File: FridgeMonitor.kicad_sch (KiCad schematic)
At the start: 26 parts, among them J1 Conn_01x03, J2 Conn_01x03, J3 Conn_01x03, J4 Conn_01x03, J6 Conn_02x04_Odd_Even, J7 USB_B_Micro, U1 ESP-01v090, U2 LM2594M-3.3

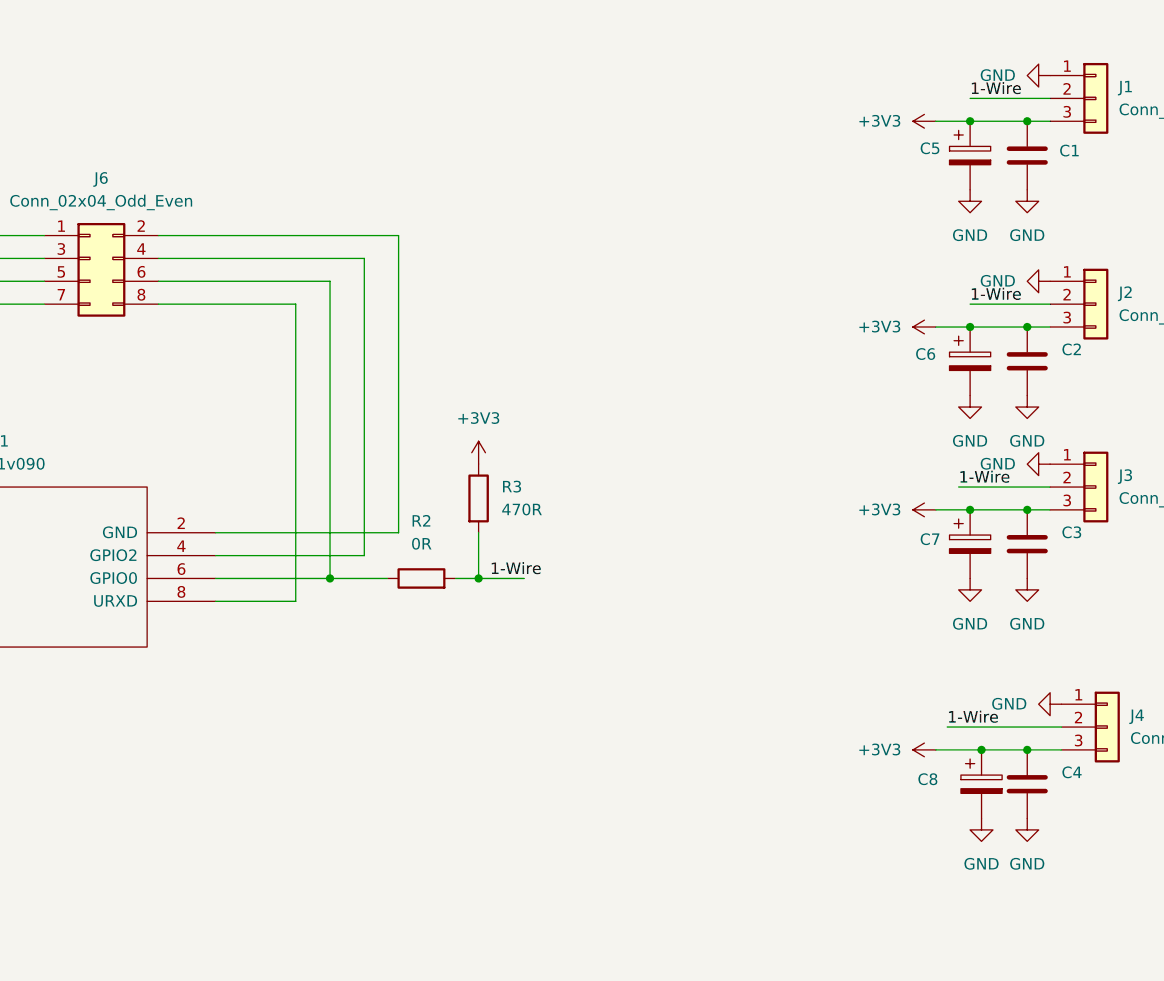
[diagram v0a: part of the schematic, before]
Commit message: For the moment all routed, except GND
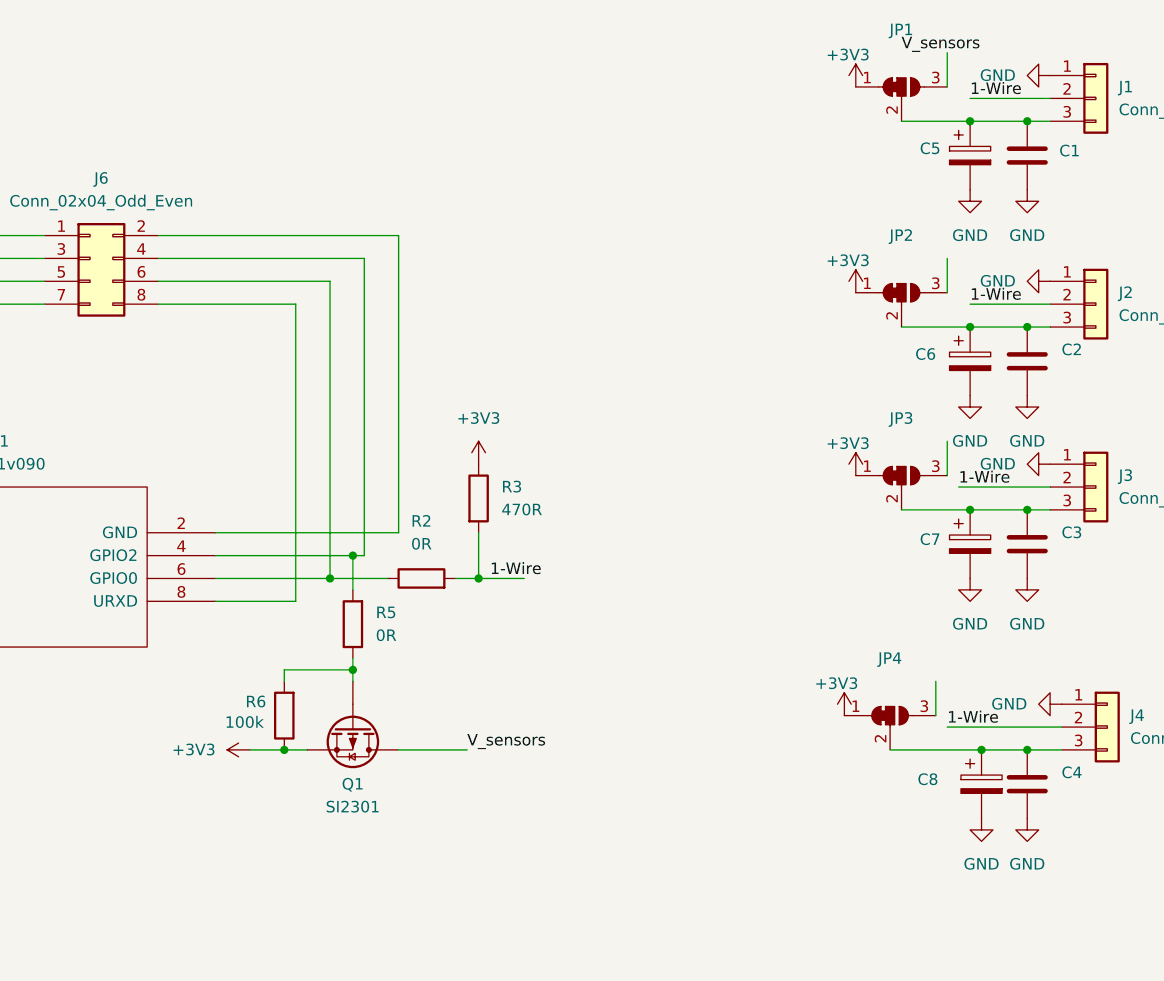
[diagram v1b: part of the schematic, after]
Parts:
- added JP1, JP2, JP3, JP4: SolderJumper_3_Bridged12, Jumper:SolderJumper-3_P1.3mm_Open_Pad1.0x1.5mm, symbol Jumper:SolderJumper_3_Bridged12
- added Q1: SI2301, Package_TO_SOT_SMD:TSOT-23, symbol Device:Q_PMOS
- added R5: 0R, Resistor_SMD:R_0805_2012Metric_Pad1.20x1.40mm_HandSolder, symbol Device:R
- added R6: 100k, Resistor_SMD:R_0805_2012Metric_Pad1.20x1.40mm_HandSolder, symbol Device:R
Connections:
- net +3V3: now also JP1.1 (A), JP2.1 (A), JP3.1 (A), JP4.1 (A), Q1.2 (S), R6.1; no longer C1.1, C2.1, C3.1, C4.1, C5.1, C6.1, C7.1, C8.1, J1.3 (Pin_3), J2.3 (Pin_3), J3.3 (Pin_3), J4.3 (Pin_3)
- net at J6.4 (Pin_4), U1.4 (GPIO2): now also R5.2
- new net: C1.1, C5.1, J1.3 (Pin_3), JP1.2 (C)
- new net: C4.1, C8.1, J4.3 (Pin_3), JP4.2 (C)
- new net: C2.1, C6.1, J2.3 (Pin_3), JP2.2 (C)
- new net: C3.1, C7.1, J3.3 (Pin_3), JP3.2 (C)
- new net: Q1.1 (G), R5.1, R6.2
- new net V_sensors: Q1.3 (D)

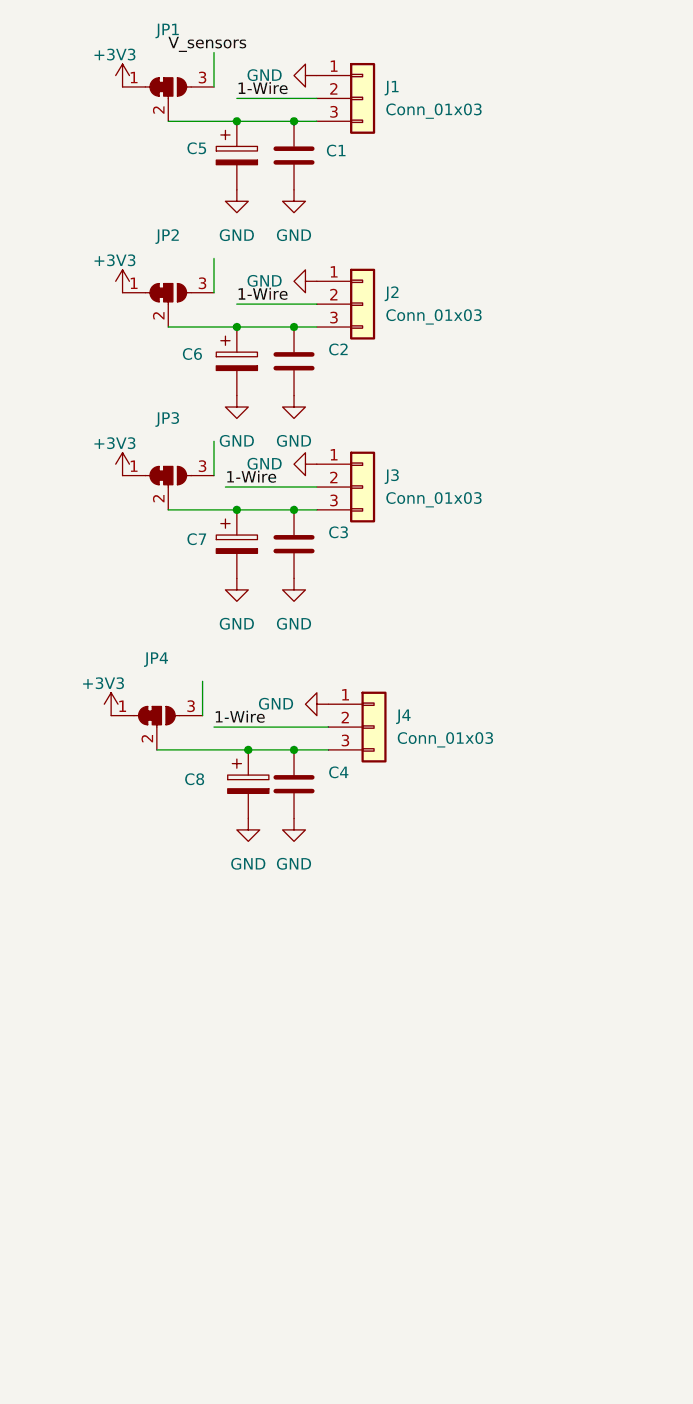
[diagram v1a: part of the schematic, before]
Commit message: All routet except ground plane plus additional footprints
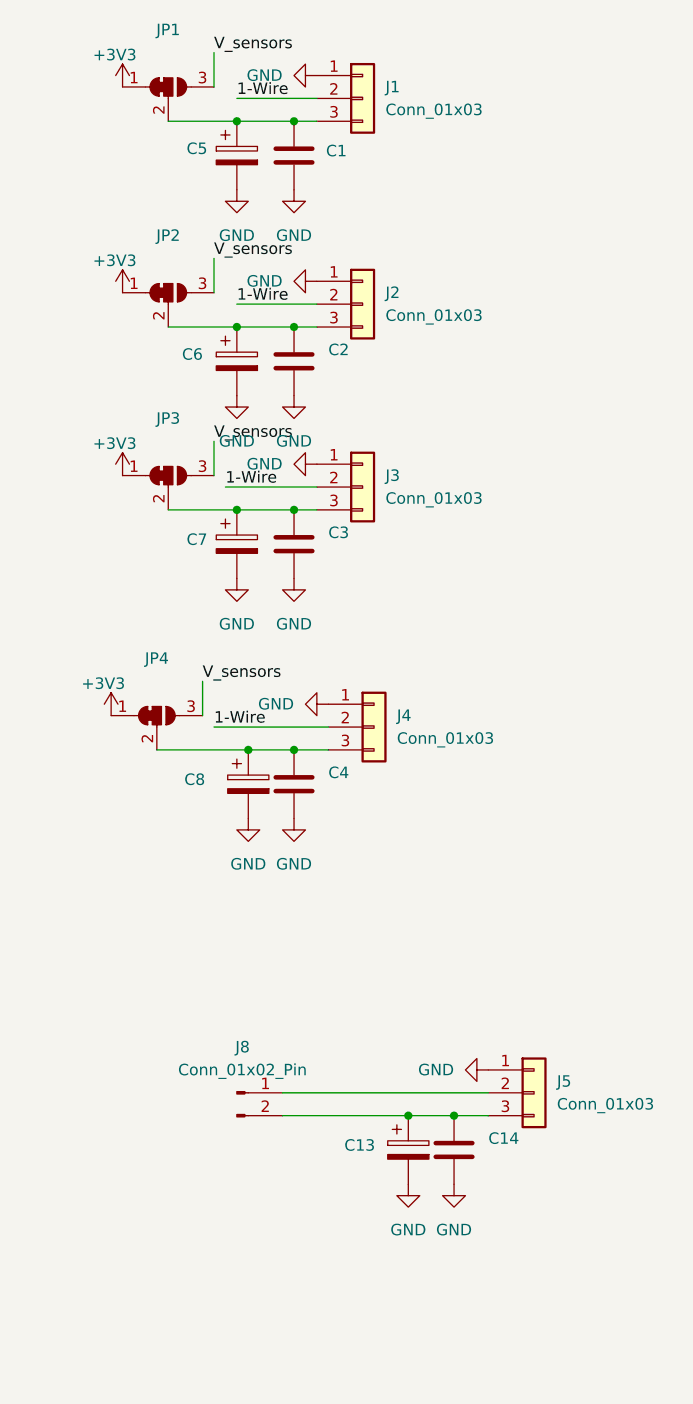
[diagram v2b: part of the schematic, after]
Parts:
- added C13: C_Polarized, Capacitor_THT:CP_Radial_D6.3mm_P2.50mm, symbol Device:C_Polarized
- added C14: C, Capacitor_SMD:C_0805_2012Metric_Pad1.18x1.45mm_HandSolder, symbol Device:C
- added J5: Conn_01x03, Connector_Phoenix_MC_HighVoltage:PhoenixContact_MC_1,5_3-G-5.08_1x03_P5.08mm_Horizontal, symbol Connector_Generic:Conn_01x03
- added J8: Conn_01x02_Pin, symbol Connector:Conn_01x02_Pin
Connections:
- net GND: now also C13.2, C14.2, J5.1 (Pin_1)
- net V_sensors: now also JP1.3 (B), JP2.3 (B), JP3.3 (B), JP4.3 (B)
- new net: J5.2 (Pin_2), J8.1 (Pin_1)
- new net: C13.1, C14.1, J5.3 (Pin_3), J8.2 (Pin_2)

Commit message: backup
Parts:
- added A1: RaspberryPi_Pico, OwnFootprints:EVB_PICO, symbol MCU_Module:RaspberryPi_Pico
- added C15: C_Polarized, Capacitor_THT:CP_Radial_D6.3mm_P2.50mm, symbol Device:C_Polarized
- added C16: C, Capacitor_SMD:C_0805_2012Metric_Pad1.18x1.45mm_HandSolder, symbol Device:C
- added J10, J9: Conn_01x02_Pin, Connector_PinSocket_2.54mm:PinSocket_1x02_P2.54mm_Vertical, symbol Connector:Conn_01x02_Pin
- added J11: Conn_01x03, Connector_Phoenix_MC_HighVoltage:PhoenixContact_MC_1,5_3-G-5.08_1x03_P5.08mm_Horizontal, symbol Connector_Generic:Conn_01x03
- J8: footprint (none) -> Connector_PinSocket_2.54mm:PinSocket_1x02_P2.54mm_Vertical
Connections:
- net GND: now also A1.13 (GND), A1.18 (GND), A1.23 (GND), A1.28 (GND), A1.3 (GND), A1.33 (AGND), A1.38 (GND), A1.8 (GND), C15.2, C16.2, J11.1 (Pin_1), J9.1 (Pin_1)
- net at C9.1, J7.1 (VBUS), U2.7 (VIN): now also J9.2 (Pin_2)
- new net: J10.1 (Pin_1), J11.2 (Pin_2)
- new net: C15.1, C16.1, J10.2 (Pin_2), J11.3 (Pin_3)

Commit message: all routed, except GND
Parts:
- removed A1: RaspberryPi_Pico, OwnFootprints:EVB_PICO, symbol MCU_Module:RaspberryPi_Pico
- added J13: Conn_01x06_Pin, Connector_PinHeader_2.54mm:PinHeader_1x06_P2.54mm_Vertical, symbol Connector:Conn_01x06_Pin
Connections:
- net +3V3: now also J13.3 (Pin_3), J13.4 (Pin_4)
- net GND: now also J13.5 (Pin_5), J13.6 (Pin_6)
- net +5V: now reaches C9.1, J7.1 (VBUS), J9.2 (Pin_2), U2.7 (VIN)
- net +5V: now also J13.1 (Pin_1), J13.2 (Pin_2)

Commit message: FIX: GND for ESP01 module
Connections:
- net GND: now also J6.2 (Pin_2), U1.2 (GND)
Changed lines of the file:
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@@
 	)
 	(junction
+		(at 137.16 71.12)
+		(diameter 0)
+		(color 0 0 0 0)
+	)
+	(junction
 		(at 44.45 144.78)
 		(diameter 0)
@@
 	(wire
 		(pts
+			(xy 137.16 83.82) (xy 137.16 71.12)
+		)
+		(stroke
+			(width 0)
+			(type default)
+		)
+	)
+	(wire
+		(pts
 			(xy 219.71 48.26) (xy 226.06 48.26)
 		)
@@
 	(wire
 		(pts
+			(xy 137.16 71.12) (xy 156.21 71.12)
+		)
+		(stroke
+			(width 0)
+			(type default)
+		)
+	)
+	(wire
+		(pts
 			(xy 215.9 87.63) (xy 215.9 91.44)
 		)
@@
 	(wire
 		(pts
-			(xy 135.89 71.12) (xy 156.21 71.12)
+			(xy 135.89 71.12) (xy 137.16 71.12)
 		)
 		(stroke
@@
 					(unit 1)
 				)
+			)
+		)
+	)
+	(symbol
+		(lib_id "power:GND")
+		(at 137.16 83.82 0)
+		(unit 1)
+		(body_style 1)
+		(exclude_from_sim no)
+		(in_bom yes)
+		(on_board yes)
+		(in_pos_files yes)
+		(dnp no)
+		(fields_autoplaced yes)
+		(property "Reference" "#PWR042"
+			(at 137.16 90.17 0)
+			(hide yes)
+			(show_name no)
+			(do_not_autoplace no)
+			(effects
+				(font
+					(size 1.27 1.27)
+				)
+			)
+		)
+		(property "Value" "GND"
+			(at 137.16 88.9 0)
+			(show_name no)
+			(do_not_autoplace no)
+			(effects
+				(font
+					(size 1.27 1.27)
+				)
+			)
+		)
+		(property "Footprint" ""
+			(at 137.16 83.82 0)
+			(hide yes)
+			(show_name no)
+			(do_not_autoplace no)
+			(effects
+				(font
+					(size 1.27 1.27)
+				)
+			)
+		)
+		(property "Datasheet" ""
+			(at 137.16 83.82 0)
+			(hide yes)
+			(show_name no)
+			(do_not_autoplace no)
+			(effects
+				(font
+					(size 1.27 1.27)
+				)
+			)
+		)
+		(property "Description" "Power symbol creates a global label with name \"GND\" , ground"
+			(at 137.16 83.82 0)
+			(hide yes)
+			(show_name no)
+			(do_not_autoplace no)
+			(effects
+				(font
+					(size 1.27 1.27)
+				)
+			)
+		)
+		(pin "1"
+		)
+		(instances
+			(project "FridgeMonitor"
+				(path "/16b7284a-799c-4c2f-acd0-53a3f6eac8c0"
+					(reference "#PWR042")
+					(unit 1)
+				)
